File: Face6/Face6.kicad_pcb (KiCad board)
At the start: 2 copper layers, 100.3 x 100.3 mm, 99 parts, among them J1 Conn_01x02_Female, J10 Conn_01x03_Female, J11 Conn_01x03_Female, J12 Conn_01x03_Female, J13 Conn_02x10_Odd_Even, J14 Conn_02x04_Counter_Clockwise, J15 Conn_02x04_Counter_Clockwise, J16 Conn_02x04_Counter_Clockwise, J17 Conn_02x04_Counter_Clockwise, J18 Conn_02x04_Counter_Clockwise, J19 Conn_02x04_Counter_Clockwise, J2 Barrel_Jack_Switch_MountingPin, J3 Conn_02x04_Counter_Clockwise, J4 Conn_01x03_Female, J5 Conn_01x03_Female, J6 Conn_02x04_Counter_Clockwise, J7 Conn_01x03_Female, J8 Conn_01x03_Female, J9 Conn_01x03_Female, SW1 SW_SPDT, SW2 SW_Push_SPDT, U1 MCP73213, U2 TPS62152, U3 TPS62153, U4 STM32WB55REV, U5 AS1115-BQFT, U6 CA56-12EWA, U7 AS1105WL-T, Y1 NX2012_32K768, Y2 Crystal_GND34

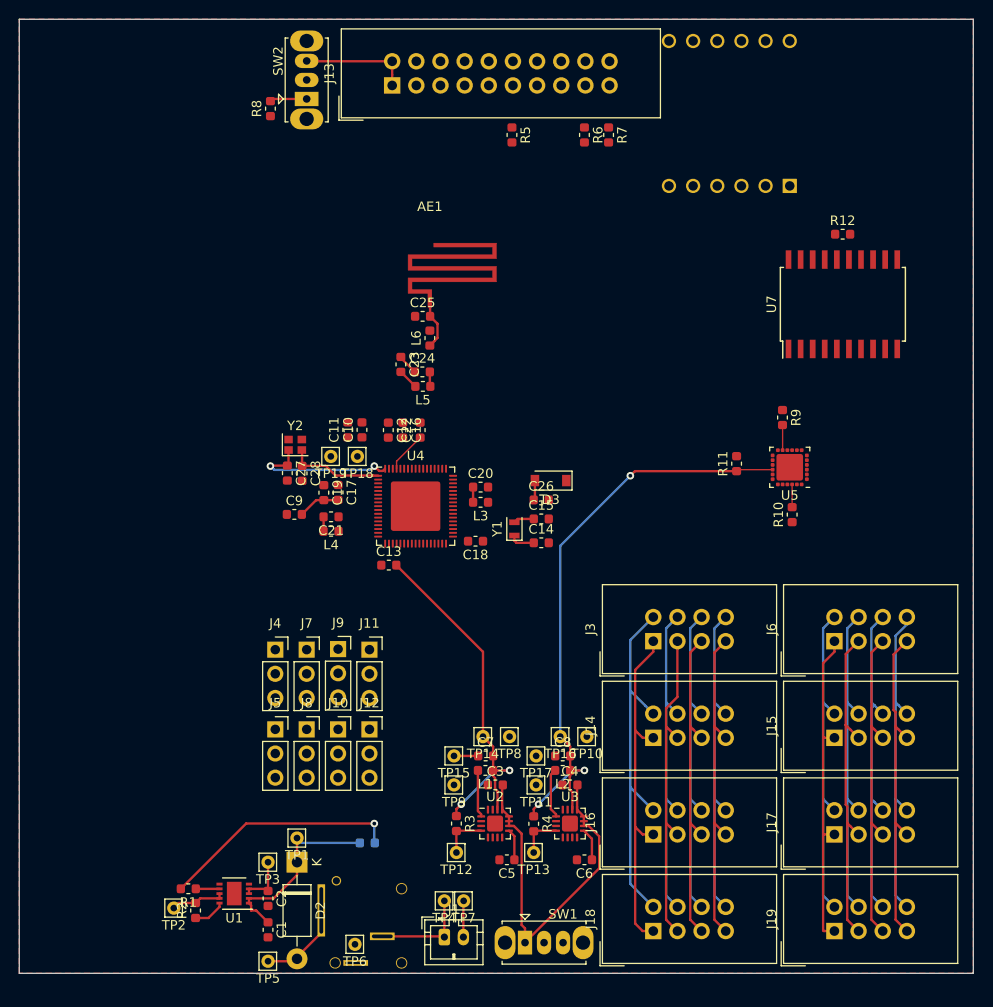
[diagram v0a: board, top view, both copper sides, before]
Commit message: Changed to multiple AS1105 for LED drivers
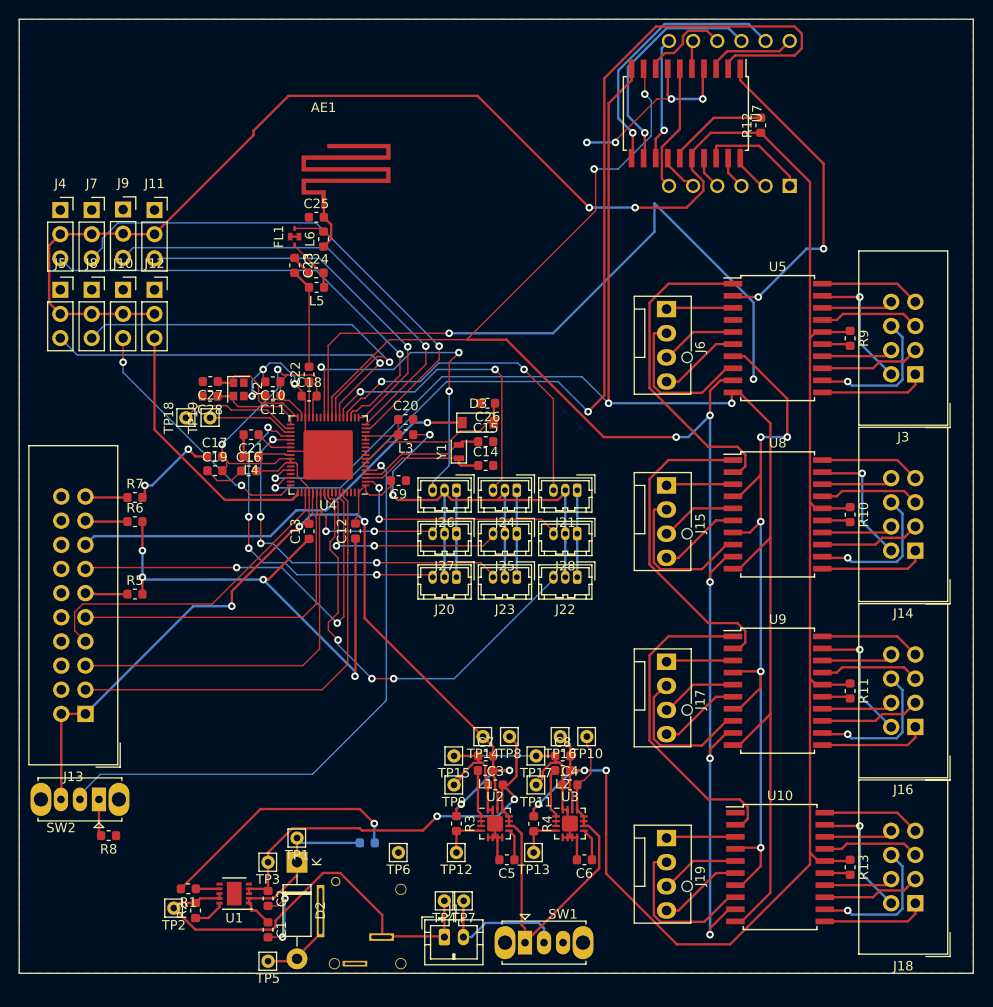
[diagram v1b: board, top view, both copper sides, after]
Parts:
- added FL1: DEA162450BT, ody-box:DEA162450BT, F.Cu at (162.3, 61.0)
- added J20: Conn_01x03_Male, Connector_Hirose:Hirose_DF13-03P-1.25DSA_1x03_P1.25mm_Vertical, F.Cu at (179.3, 96.8)
- added J21: Conn_01x03_Male, Connector_Hirose:Hirose_DF13-03P-1.25DSA_1x03_P1.25mm_Vertical, F.Cu at (192.0, 87.6)
- added J22: Conn_01x03_Male, Connector_Hirose:Hirose_DF13-03P-1.25DSA_1x03_P1.25mm_Vertical, F.Cu at (192.0, 96.8)
- added J23: Conn_01x03_Male, Connector_Hirose:Hirose_DF13-03P-1.25DSA_1x03_P1.25mm_Vertical, F.Cu at (185.7, 96.8)
- added J24: Conn_01x03_Male, Connector_Hirose:Hirose_DF13-03P-1.25DSA_1x03_P1.25mm_Vertical, F.Cu at (185.7, 87.6)
- added J25: Conn_01x03_Male, Connector_Hirose:Hirose_DF13-03P-1.25DSA_1x03_P1.25mm_Vertical, F.Cu at (185.7, 92.2)
- added J26: Conn_01x03_Male, Connector_Hirose:Hirose_DF13-03P-1.25DSA_1x03_P1.25mm_Vertical, F.Cu at (179.3, 87.6)
- added J27: Conn_01x03_Male, Connector_Hirose:Hirose_DF13-03P-1.25DSA_1x03_P1.25mm_Vertical, F.Cu at (179.3, 92.2)
- added J28: Conn_01x03_Male, Connector_Hirose:Hirose_DF13-03P-1.25DSA_1x03_P1.25mm_Vertical, F.Cu at (192.0, 92.2)
- added R13: 9.53k, Resistor_SMD:R_0603_1608Metric, F.Cu at (220.7, 127.3)
- added U10: AS1105WL-T, Package_SO:SOIC-20W_7.5x12.8mm_P1.27mm, F.Cu at (213.4, 127.3)
- added U8: AS1105WL-T, Package_SO:SOIC-20W_7.5x12.8mm_P1.27mm, F.Cu at (213.1, 90.2)
- added U9: AS1105WL-T, Package_SO:SOIC-20W_7.5x12.8mm_P1.27mm, F.Cu at (213.1, 108.7)
- J14, J16, J18, J3: value Conn_02x04_Counter_Clockwise -> Conn_02x04_Odd_Even
- J15, J17, J19, J6: value Conn_02x04_Counter_Clockwise -> Conn_01x04; footprint Connector_IDC:IDC-Header_2x04_P2.54mm_Vertical -> Connector:FanPinHeader_1x04_P2.54mm_Vertical
- J2: value Barrel_Jack_Switch_MountingPin -> Barrel_Jack_Switch
- R10, R9: value 4.7k -> 9.53k
- U5: value AS1115-BQFT -> AS1105WL-T; footprint Package_DFN_QFN:TQFN-24-1EP_4x4mm_P0.5mm_EP2.8x2.8mm_PullBack -> Package_SO:SOIC-20W_7.5x12.8mm_P1.27mm
- moved R8 78.3 mm to (142.7, 124.0), turned to 180 degrees
- moved SW2 76.8 mm to (141.7, 120.1), turned to 180 degrees
- moved J13 73.5 mm to (140.3, 111.2), turned to 180 degrees
- moved R7 62.7 mm to (145.5, 88.4), turned to 0 degrees
- moved R5 62.5 mm to (145.5, 98.6), turned to 0 degrees
- moved R6 62.4 mm to (145.5, 90.9), turned to 0 degrees
- moved J11 51.5 mm to (147.6, 58.2)
- moved J4 51.5 mm to (137.7, 58.2)
- moved J7 51.5 mm to (141.0, 58.2)
- moved J10 51.5 mm to (144.3, 66.5)
- moved J12 51.5 mm to (147.6, 66.5)
- moved J5 51.5 mm to (137.7, 66.5)
- moved J8 51.5 mm to (141.0, 66.5)
- moved J9 51.5 mm to (144.3, 58.1)
- moved J3 39.3 mm to (227.6, 75.4), turned to 180 degrees
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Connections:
- net DIG0_0 renamed DIG0
- net DIG1_0 renamed DIG1
- net DIG2_0 renamed DIG2
- net DIG3_0 renamed DIG3
- net JSTM renamed JTMS
- net SEGA_0 renamed SEGA
- net SEGB_0 renamed SEGB
- net SEGC_0 renamed SEGC
- net SEGDP_0 renamed SEGDP
- net SEGD_0 renamed SEGD
- net SEGE_0 renamed SEGE
- net SEGF_0 renamed SEGF
- net SEGG_0 renamed SEGG
- J12 pad 3: /Connectors.sch/SERVO8 -> /STM32/PWM4_TM1
- J14 pad 1: /Connectors.sch/SEGA -> /Connectors.sch/SEGA_1
- J14 pad 2: /Connectors.sch/SEGB -> /Sensors/SEGDP_1
- J14 pad 3: /Connectors.sch/SEGC -> /Connectors.sch/SEGB_1
- J14 pad 4: /Connectors.sch/SEGD -> /Connectors.sch/SEGG_1
- J14 pad 5: /Connectors.sch/SEGE -> /Connectors.sch/SEGC_1
- J14 pad 6: /Connectors.sch/SEGF -> /Connectors.sch/SEGF_1
- J14 pad 7: /Connectors.sch/SEGG -> /Connectors.sch/SEGD_1
- J14 pad 8: /Sensors/SEGDP -> /Connectors.sch/SEGE_1
- J15 pad 1: /Connectors.sch/DIG0 -> /Connectors.sch/DIG0_1
- J15 pad 2: /Connectors.sch/DIG1 -> /Connectors.sch/DIG1_1
- J15 pad 3: /Connectors.sch/DIG2 -> /Connectors.sch/DIG2_1
- J15 pad 4: /Connectors.sch/DIG3 -> /Connectors.sch/DIG3_1
- J16 pad 1: /Connectors.sch/SEGA -> /Connectors.sch/SEGA_2
- J16 pad 2: /Connectors.sch/SEGB -> /Sensors/SEGDP_2
- J16 pad 3: /Connectors.sch/SEGC -> /Connectors.sch/SEGB_2
- J16 pad 4: /Connectors.sch/SEGD -> /Connectors.sch/SEGG_2
- J16 pad 5: /Connectors.sch/SEGE -> /Connectors.sch/SEGC_2
- J16 pad 6: /Connectors.sch/SEGF -> /Connectors.sch/SEGF_2
- J16 pad 7: /Connectors.sch/SEGG -> /Connectors.sch/SEGD_2
- J16 pad 8: /Sensors/SEGDP -> /Connectors.sch/SEGE_2
- J17 pad 1: /Connectors.sch/DIG0 -> /Connectors.sch/DIG0_2
- J17 pad 2: /Connectors.sch/DIG1 -> /Connectors.sch/DIG1_2
- J17 pad 3: /Connectors.sch/DIG2 -> /Connectors.sch/DIG2_2
- J17 pad 4: /Connectors.sch/DIG3 -> /Connectors.sch/DIG3_2
- J18 pad 1: /Connectors.sch/SEGA -> /Connectors.sch/SEGA_3
- J18 pad 2: /Connectors.sch/SEGB -> /Sensors/SEGDP_3
- J18 pad 3: /Connectors.sch/SEGC -> /Connectors.sch/SEGB_3
- J18 pad 4: /Connectors.sch/SEGD -> /Connectors.sch/SEGG_3
- J18 pad 5: /Connectors.sch/SEGE -> /Connectors.sch/SEGC_3
- J18 pad 6: /Connectors.sch/SEGF -> /Connectors.sch/SEGF_3
- J18 pad 7: /Connectors.sch/SEGG -> /Connectors.sch/SEGD_3
- J18 pad 8: /Sensors/SEGDP -> /Connectors.sch/SEGE_3
- J19 pad 1: /Connectors.sch/DIG0 -> /Connectors.sch/DIG0_3
- J19 pad 2: /Connectors.sch/DIG1 -> /Connectors.sch/DIG1_3
- J19 pad 3: /Connectors.sch/DIG2 -> /Connectors.sch/DIG2_3
- J19 pad 4: /Connectors.sch/DIG3 -> /Connectors.sch/DIG3_3
- J3 pad 1: /Connectors.sch/SEGA -> /Connectors.sch/SEGA_0
- J3 pad 2: /Connectors.sch/SEGB -> /Sensors/SEGDP_0
- J3 pad 3: /Connectors.sch/SEGC -> /Connectors.sch/SEGB_0
- J3 pad 4: /Connectors.sch/SEGD -> /Connectors.sch/SEGG_0
- J3 pad 5: /Connectors.sch/SEGE -> /Connectors.sch/SEGC_0
- J3 pad 6: /Connectors.sch/SEGF -> /Connectors.sch/SEGF_0
- J3 pad 7: /Connectors.sch/SEGG -> /Connectors.sch/SEGD_0
- J3 pad 8: /Sensors/SEGDP -> /Connectors.sch/SEGE_0
- J6 pad 1: /Connectors.sch/DIG0 -> /Connectors.sch/DIG0_0
- J6 pad 2: /Connectors.sch/DIG1 -> /Connectors.sch/DIG1_0
- J6 pad 3: /Connectors.sch/DIG2 -> /Connectors.sch/DIG2_0
- J6 pad 4: /Connectors.sch/DIG3 -> /Connectors.sch/DIG3_0
- R10 pad 2: /Sensors/SDA -> Net-(R10-Pad2)
- R9 pad 2: /Sensors/SCL -> Net-(R9-Pad2)
- U4 pad 2: Net-(U4-Pad2) -> /STM32/GPIO_EXT13
- U4 pad 21: Net-(U4-Pad21) -> /STM32/GPIO_EXT6
- U4 pad 22: Net-(U4-Pad22) -> /STM32/GPIO_EXT7
- U4 pad 27: Net-(U4-Pad27) -> /STM32/GPIO_EXT2
- U4 pad 28: /STM32/TX1 -> /STM32/LPRX1
- U4 pad 29: /STM32/RX1 -> /STM32/LPTX1
- U4 pad 38: Net-(U4-Pad38) -> /STM32/GPIO_EXT0
- U4 pad 39: Net-(U4-Pad39) -> /STM32/GPIO_EXT1
- U4 pad 52: Net-(U4-Pad52) -> /STM32/PWM4_TM1
- U4 pad 58: /STM32/GPIO3_2 -> /STM32/GPIO_EXT10
- U4 pad 59: /STM32/GPIO4_2 -> /STM32/GPIO_EXT11
- U4 pad 6: /Sensors/SCL -> /STM32/SCL1
- U4 pad 60: /STM32/GPIO5_2 -> /STM32/GPIO_EXT12
- U4 pad 65: /STM32/GPIO6_2 -> /STM32/GPIO3_2
- U4 pad 66: /STM32/GPIO7_2 -> /STM32/TX1
- U4 pad 67: /STM32/GPIO8_2 -> /STM32/RX1
- U4 pad 7: /Sensors/SDA -> /STM32/SDA1
- U5 pad 1: /Connectors.sch/DIG2 -> Net-(U5-Pad1)
- U5 pad 10: Net-(R11-Pad2) -> /STM32/SCK
- U5 pad 11: /Sensors/SCL -> /Connectors.sch/SEGA_0
- U5 pad 12: /Connectors.sch/SEGA -> /Connectors.sch/SEGF_0
- U5 pad 13: /Connectors.sch/SEGF -> /Connectors.sch/SEGB_0
- U5 pad 14: /Connectors.sch/SEGB -> /Connectors.sch/SEGG_0
- U5 pad 15: /Connectors.sch/SEGG -> Net-(R9-Pad2)
- U5 pad 17: /Connectors.sch/SEGC -> /Connectors.sch/SEGC_0
- U5 pad 18: /Connectors.sch/SEGE -> /Connectors.sch/SEGE_0
- U5 pad 19: /Sensors/SEGDP -> /Sensors/SEGDP_0
- U5 pad 2: /Connectors.sch/DIG3 -> Net-(U5-Pad2)
- U5 pad 20: /Connectors.sch/SEGD -> /Connectors.sch/SEGD_0
- U5 pad 3: GND -> /Connectors.sch/DIG0_0
- U5 pad 4: /Connectors.sch/DIG4 -> GND
- U5 pad 5: /Connectors.sch/DIG5 -> /Connectors.sch/DIG2_0
- U5 pad 6: /Connectors.sch/DIG6 -> /Connectors.sch/DIG3_0
- U5 pad 7: /Connectors.sch/DIG7 -> GND
- U5 pad 8: Net-(U5-Pad8) -> /Connectors.sch/DIG1_0
- U5 pad 9: Net-(U5-Pad9) -> /STM32/GPIO0_2
- U7 pad 1: Net-(U7-Pad1) -> Net-(U5-Pad2)
- U7 pad 4: Net-(U7-Pad4) -> GND
- U7 pad 7: Net-(U7-Pad7) -> GND
- U7 pad 9: /STM32/GPIO1_2 -> /STM32/GPIO0_2
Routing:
- net GND: track 4.73 -> 282.6 mm, vias 0 -> 20
- net +5V: track 63.2 -> 267.5 mm, vias 3 -> 5
- net /STM32/SCK: track 0.00 -> 163.1 mm, vias 0 -> 3
- net /STM32/GPIO0_2: track 0.00 -> 160.4 mm, vias 0 -> 7
- net +3V3: track 55.9 -> 214.5 mm, vias 2 -> 9
- net /STM32/MOSI: track 0.00 -> 110.6 mm, vias 0 -> 2
- net /STM32/GPIO1_2: track 0.00 -> 72.8 mm, vias 0 -> 2
- net Net-(SW2-Pad2): track 0.00 -> 63.6 mm, vias 0 -> 1
- net /STM32/PWM2_TM2: track 0.00 -> 56.2 mm, vias 0 -> 1
- net /STM32/PWM1_TM2: track 0.00 -> 49.4 mm, vias 0 -> 1
- net /STM32/PWM3_TM2: track 0.00 -> 47.4 mm, vias 0 -> 1
- net nJTRST: track 0.00 -> 47.0 mm
- net /STM32/GPIO_EXT11: track 0.00 -> 46.8 mm, vias 0 -> 3
- net nSRST: track 0.00 -> 45.0 mm, vias 0 -> 1
- net /BatteryCharger/BAT+: track 44.6 -> 88.3 mm, vias 0 -> 2
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
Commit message: Separated Li-ion charger to face and optimized
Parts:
- removed C1, C2: 1uF, Capacitor_SMD:C_0603_1608Metric
- removed D1: Blue, LED_SMD:LED_0603_1608Metric
- removed R1: 1k, Resistor_SMD:R_0603_1608Metric
- removed R2: 1.1k 1% E96, Resistor_SMD:R_0603_1608Metric
- removed TP1, TP2, TP3: TestPoint, Connector_Pin:Pin_D0.7mm_L6.5mm_W1.8mm_FlatFork
- removed U1: MCP73213, Package_DFN_QFN:DFN-10-1EP_3x3mm_P0.5mm_EP1.55x2.48mm
- added J29: Conn_01x03_Male, Connector_Hirose:Hirose_DF13-03P-1.25DSA_1x03_P1.25mm_Vertical, F.Cu at (156.0, 134.9)
- D3: footprint Diode_SMD:D_SOD-123 -> Diode_SMD:D_SOD-523
- J10, J11, J12, J4, J5, J7, J8, J9: value Conn_01x03_Female -> Conn_01x03_Male; footprint Connector_PinSocket_2.54mm:PinSocket_1x03_P2.54mm_Vertical -> Connector_PinHeader_2.54mm:PinHeader_1x03_P2.54mm_Vertical
- L3: value FCM1608KF-601T03 -> KMZ1608
- R10, R11, R13, R9: value 9.53k -> 22.6k
- R12: value 9.53k -> 28k
- SW2: value SW_Push_SPDT -> SW_SPDT
- TP10, TP11, TP12, TP13, TP14, TP15, TP16, TP17, TP18, TP19, TP4, TP5, TP6, TP7, TP8, TP9: footprint Connector_Pin:Pin_D0.7mm_L6.5mm_W1.8mm_FlatFork -> TestPoint:TestPoint_THTPad_D1.0mm_Drill0.5mm
- Y2: value Crystal_GND34 -> NX3225SA-32MHz
- moved D3 0.76 mm to (182.4, 80.5)
- moved TP6 0.72 mm to (173.7, 126.2)
- moved TP13 0.25 mm to (187.5, 126.0)
- moved J9 0.11 mm to (144.3, 58.2)
- turned TP18 to 0 degrees
- turned TP19 to 0 degrees
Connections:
- net /BatteryCharger/BAT+ renamed /Connectors.sch/BAT+
- D2 pad 1: /BatteryCharger/12V -> /Connectors.sch/12V
- J1 pad 1: /BatteryCharger/BAT- -> /Connectors.sch/BAT-
- J2 pad 2: GND -> /Connectors.sch/BAT-
- J2 pad 3: /BatteryCharger/BAT- -> GND
- J21 pad 3: /STM32/GPIO_EXT6 -> /STM32/GPIO_EXT4
- J22 pad 3: /STM32/GPIO_EXT11 -> /STM32/GPIO_EXT7
- J24 pad 3: /STM32/GPIO_EXT7 -> /STM32/GPIO_EXT5
- J25 pad 3: /STM32/GPIO_EXT12 -> /STM32/GPIO_EXT10
- J27 pad 3: /STM32/GPIO_EXT10 -> /STM32/GPIO_EXT6
- J28 pad 3: /STM32/GPIO_EXT13 -> /STM32/GPIO_EXT11
- TP4 pad 1: /BatteryCharger/BAT- -> /Connectors.sch/BAT-
- TP6 pad 1: GND -> /Connectors.sch/BAT-
- U4 pad 40: Net-(U4-Pad40) -> /STM32/GPIO_EXT4
- U4 pad 65: /STM32/GPIO3_2 -> /STM32/GPIO_EXT5
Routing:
- net /STM32/GPIO_EXT4: track 0.00 -> 55.4 mm, vias 0 -> 4
- net /BatteryCharger/BAT-: track 45.9 -> 0.00 mm
- net /Connectors.sch/BAT-: track 0.00 -> 44.1 mm
- net Net-(D1-Pad1): track 26.5 -> 0.00 mm, vias 1 -> 0
- net /STM32/GPIO_EXT13: track 24.1 -> 0.00 mm, vias 2 -> 0
- net /STM32/GPIO_EXT10: track 15.6 -> 38.3 mm
- net /BatteryCharger/12V: track 20.4 -> 0.00 mm
- net /STM32/GPIO_EXT5: track 0.00 -> 20.0 mm, vias 0 -> 4
- net /STM32/GPIO_EXT6: track 35.6 -> 54.0 mm
- net /STM32/GPIO_EXT12: track 23.5 -> 6.31 mm, vias 2 -> 1
- net /STM32/GPIO_EXT7: track 32.0 -> 48.5 mm
- net /Connectors.sch/12V: track 0.00 -> 10.6 mm
- net /STM32/GPIO0_2: track 160.4 -> 168.0 mm
- net /Connectors.sch/BAT+: track 88.3 -> 93.7 mm, vias 2 -> 0
- net /STM32/GPIO_EXT1: track 39.4 -> 43.6 mm
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
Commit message: Changed Regulatros to cheaper ones.
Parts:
- removed C7, C8: 22uF, Capacitor_SMD:C_0603_1608Metric
- removed L1, L2: 2.2uH, Inductor_SMD:L_0603_1608Metric
- removed R3, R4: 100k, Resistor_SMD:R_0603_1608Metric
- removed TP10, TP11, TP12, TP13, TP14, TP15, TP16, TP17, TP9: TestPoint, TestPoint:TestPoint_THTPad_D1.0mm_Drill0.5mm
- added C1: 0.1uF, Capacitor_SMD:C_0603_1608Metric, F.Cu at (148.3, 133.9)
- added C2: 0.33uF, Capacitor_SMD:C_0603_1608Metric, F.Cu at (189.7, 126.5)
- added TP1: TestPoint, TestPoint:TestPoint_THTPad_D1.0mm_Drill0.5mm, F.Cu at (153.4, 130.3)
- added TP2: TestPoint, TestPoint:TestPoint_THTPad_D1.0mm_Drill0.5mm, F.Cu at (138.4, 130.0)
- added TP3: TestPoint, TestPoint:TestPoint_THTPad_D1.0mm_Drill0.5mm, F.Cu at (195.8, 129.0)
- added U1: LD1117S33TR_SOT223, Package_TO_SOT_SMD:SOT-223-3_TabPin2, F.Cu at (143.8, 131.3)
- C3: value 10uF -> 0.33uF
- C5, C6: value 3.3nF -> 0.1uF
- U2: value TPS62152 -> L7805; footprint Package_DFN_QFN:VQFN-16-1EP_3x3mm_P0.5mm_EP1.68x1.68mm -> Package_TO_SOT_THT:TO-220-3_Vertical
- U3: value TPS62153 -> L7805; footprint Package_DFN_QFN:VQFN-16-1EP_3x3mm_P0.5mm_EP1.68x1.68mm -> Package_TO_SOT_THT:TO-220-3_Vertical
- moved C4 54.9 mm to (138.4, 133.6), turned to 90 degrees
- moved TP4 20.6 mm to (157.5, 131.1)
- moved TP8 15.5 mm to (185.4, 129.0)
- moved U3 13.7 mm to (177.8, 120.4)
- moved C6 10.4 mm to (182.4, 126.5), turned to 0 degrees
- moved C3 9.13 mm to (178.8, 126.5), turned to 180 degrees
- moved C5 8.66 mm to (193.3, 126.5), turned to 0 degrees
- moved TP6 6.29 mm to (178.1, 130.8)
- moved U2 5.80 mm to (188.7, 120.4)
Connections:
- C4 pad 2: /Connectors.sch/BAT+ -> +3V3
- C5 pad 1: Net-(C5-Pad1) -> GND
- C5 pad 2: GND -> +5VP
- C6 pad 1: Net-(C6-Pad1) -> GND
- C6 pad 2: GND -> +5V
- TP8 pad 1: /Connectors.sch/BAT+ -> +5V
- U2 pad 1: Net-(L1-Pad2) -> /Connectors.sch/BAT+
- U2 pad 2: Net-(L1-Pad2) -> GND
- U2 pad 3: Net-(L1-Pad2) -> +5VP
- U3 pad 1: Net-(L2-Pad2) -> /Connectors.sch/BAT+
- U3 pad 2: Net-(L2-Pad2) -> GND
- U3 pad 3: Net-(L2-Pad2) -> +5V
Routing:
- net GND: track 281.0 -> 309.4 mm, vias 18 -> 20
- net /Connectors.sch/BAT+: track 93.7 -> 78.8 mm
- net +3V3: track 215.1 -> 204.9 mm, vias 9 -> 7
- net +5VP: track 0.00 -> 9.48 mm
- net /Connectors.sch/BAT-: track 44.1 -> 35.3 mm
- net Net-(L2-Pad2): track 6.26 -> 0.00 mm
- net Net-(L1-Pad2): track 5.98 -> 0.00 mm
- net Net-(R3-Pad2): track 4.88 -> 0.00 mm
- net Net-(R4-Pad2): track 4.61 -> 0.00 mm
- net Net-(C6-Pad1): track 3.41 -> 0.00 mm
- net Net-(C5-Pad1): track 3.30 -> 0.00 mm
- net /STM32/GPIO_EXT11: track 49.8 -> 52.1 mm
- net +5V: track 267.5 -> 268.6 mm, vias 5 -> 2
